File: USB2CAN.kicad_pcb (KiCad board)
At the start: 2 copper layers, 53.3 x 44.9 mm, 94 parts, among them J1 Conn_01x04, J2 Conn_01x02, J3 Conn_01x02, J4 Conn_01x02, J5 Conn_01x02, U1 HX9193, U10 SL2.1S, U2 STM32F072C8Tx, U3 TJA1051T-3, U4 STM32F072C8Tx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

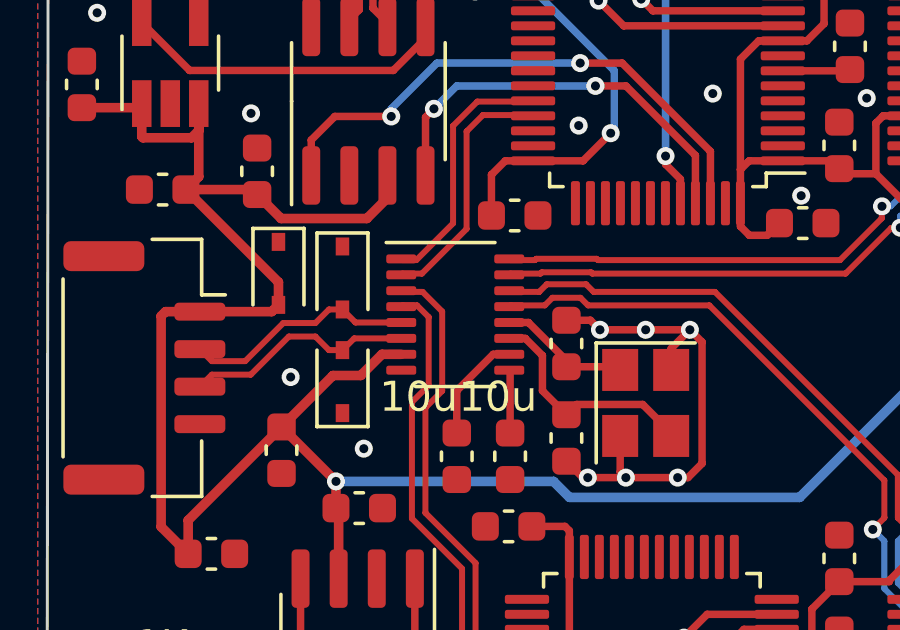
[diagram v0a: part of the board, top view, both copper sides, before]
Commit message: Turn overall Lib to local Lib to avoid incorrect display of schematics
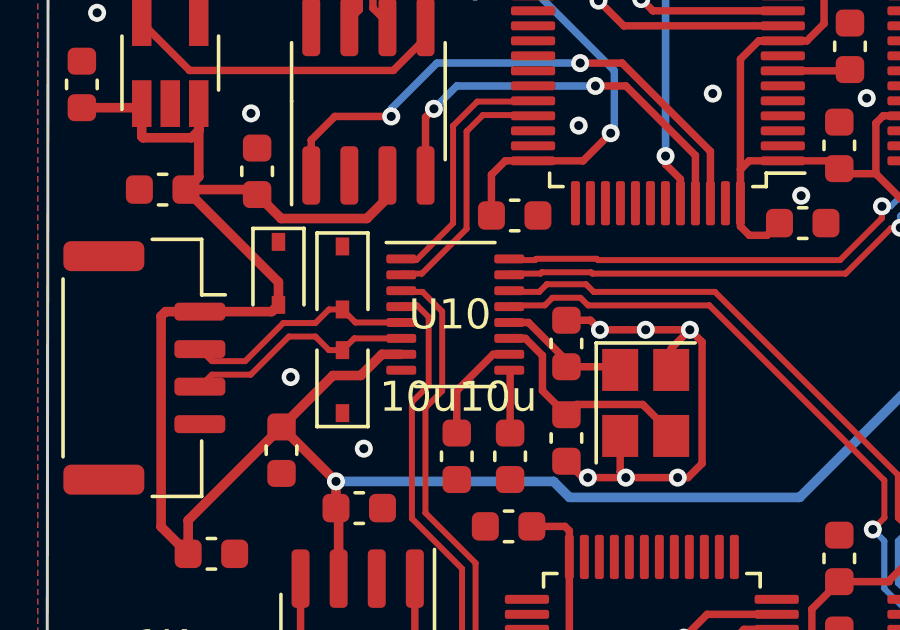
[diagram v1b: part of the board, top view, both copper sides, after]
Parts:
- removed REF** (x4): MountingHole_2.7mm_M2.5, MountingHole:MountingHole_2.7mm_M2.5
- added H1: MountingHole, MountingHole:MountingHole_2.7mm_M2.5, F.Cu at (85.2, 28.9)
- added H2: MountingHole, MountingHole:MountingHole_2.7mm_M2.5, F.Cu at (131.6, 28.9)
- added H3: MountingHole, MountingHole:MountingHole_2.7mm_M2.5, F.Cu at (131.6, 67.0)
- added H4: MountingHole, MountingHole:MountingHole_2.7mm_M2.5, F.Cu at (85.2, 67.0)
- U10: footprint MyLib:SL2.1S-SSOP-16 -> PcbLib:SL2.1S-SSOP-16
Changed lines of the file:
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@@
     )
   )
-  (footprint "MountingHole:MountingHole_2.7mm_M2.5" (layer "F.Cu")
-    (at 131.572 28.8544)
-    (descr "Mounting Hole 2.7mm, no annular, M2.5")
-    (tags "mounting hole 2.7mm no annular m2.5")
-    (attr exclude_from_pos_files exclude_from_bom)
-    (fp_text reference "REF**" (at 0 -3.7) (layer "F.SilkS") hide
-      (effects (font (size 1 1) (thickness 0.15)))
-    )
-    (fp_text value "MountingHole_2.7mm_M2.5" (at 0 3.7) (layer "F.Fab")
-      (effects (font (size 1 1) (thickness 0.15)))
-    )
-    (fp_text user "${REFERENCE}" (at 0.3 0) (layer "F.Fab")
-      (effects (font (size 1 1) (thickness 0.15)))
-    )
-    (fp_circle (center 0 0) (end 2.7 0) (layer "Cmts.User") (width 0.15) (fill none))
-    (fp_circle (center 0 0) (end 2.95 0) (layer "F.CrtYd") (width 0.05) (fill none))
-    (pad "" np_thru_hole circle locked (at 0 0) (size 2.7 2.7) (drill 2.7) (layers *.Cu *.Mask))
-  )
   (footprint "Resistor_SMD:R_0603_1608Metric" (layer "F.Cu")
     (at 102.0064 31.0388 180)
@@
     )
   )
-  (footprint "MyLib:SL2.1S-SSOP-16" (layer "F.Cu")
+  (footprint "PcbLib:SL2.1S-SSOP-16" (layer "F.Cu")
     (at 95.4532 45.8216)
     (property "Sheetfile" "USB_HUB.kicad_sch")
     (property "Sheetname" "USB_HUB")
     (attr smd)
-    (fp_text reference "U10" (at -0.175 0 unlocked) (layer "F.SilkS") hide
+    (fp_text reference "U10" (at -0.175 0 unlocked) (layer "F.SilkS")
       (effects (font (size 1 1) (thickness 0.15)))
     )
@@
     )
   )
+  (footprint "MountingHole:MountingHole_2.7mm_M2.5" (layer "F.Cu")
+    (at 85.1916 28.8544)
+    (descr "Mounting Hole 2.7mm, no annular, M2.5")
+    (tags "mounting hole 2.7mm no annular m2.5")
+    (property "Sheetfile" "USB2CAN.kicad_sch")
+    (property "Sheetname" "")
+    (attr exclude_from_pos_files)
+    (fp_text reference "H1" (at 0 -3.7) (layer "F.SilkS") hide
+      (effects (font (size 1 1) (thickness 0.15)))
+    )
+    (fp_text value "MountingHole" (at 0 3.7) (layer "F.Fab")
+      (effects (font (size 1 1) (thickness 0.15)))
+    )
+    (fp_text user "${REFERENCE}" (at 0.3 0) (layer "F.Fab")
+      (effects (font (size 1 1) (thickness 0.15)))
+    )
+    (fp_circle (center 0 0) (end 2.7 0) (layer "Cmts.User") (width 0.15) (fill none))
+    (fp_circle (center 0 0) (end 2.95 0) (layer "F.CrtYd") (width 0.05) (fill none))
+    (pad "" np_thru_hole circle locked (at 0 0) (size 2.7 2.7) (drill 2.7) (layers *.Cu *.Mask))
+  )
   (footprint "Connector_JST:JST_GH_SM02B-GHS-TB_1x02-1MP_P1.25mm_Horizontal" (layer "F.Cu")
     (at 92.202 67.4116)
@@
     )
   )
-  (footprint "MountingHole:MountingHole_2.7mm_M2.5" (layer "F.Cu")
-    (at 85.1916 66.9544)
-    (descr "Mounting Hole 2.7mm, no annular, M2.5")
-    (tags "mounting hole 2.7mm no annular m2.5")
-    (attr exclude_from_pos_files exclude_from_bom)
-    (fp_text reference "REF**" (at 0 -3.7) (layer "F.SilkS") hide
-      (effects (font (size 1 1) (thickness 0.15)))
-    )
-    (fp_text value "MountingHole_2.7mm_M2.5" (at 0 3.7) (layer "F.Fab")
-      (effects (font (size 1 1) (thickness 0.15)))
-    )
-    (fp_text user "${REFERENCE}" (at 0.3 0) (layer "F.Fab")
-      (effects (font (size 1 1) (thickness 0.15)))
-    )
-    (fp_circle (center 0 0) (end 2.7 0) (layer "Cmts.User") (width 0.15) (fill none))
-    (fp_circle (center 0 0) (end 2.95 0) (layer "F.CrtYd") (width 0.05) (fill none))
-    (pad "" np_thru_hole circle locked (at 0 0) (size 2.7 2.7) (drill 2.7) (layers *.Cu *.Mask))
-  )
   (footprint "Capacitor_SMD:C_0603_1608Metric" (layer "F.Cu")
     (at 85.6996 41.656 180)
@@
     )
   )
+  (footprint "MountingHole:MountingHole_2.7mm_M2.5" (layer "F.Cu")
+    (at 131.572 66.9544)
+    (descr "Mounting Hole 2.7mm, no annular, M2.5")
+    (tags "mounting hole 2.7mm no annular m2.5")
+    (property "Sheetfile" "USB2CAN.kicad_sch")
+    (property "Sheetname" "")
+    (attr exclude_from_pos_files)
+    (fp_text reference "H3" (at 0 -3.7) (layer "F.SilkS") hide
+      (effects (font (size 1 1) (thickness 0.15)))
+    )
+    (fp_text value "MountingHole" (at 0 3.7) (layer "F.Fab")
+      (effects (font (size 1 1) (thickness 0.15)))
+    )
+    (fp_text user "${REFERENCE}" (at 0.3 0) (layer "F.Fab")
+      (effects (font (size 1 1) (thickness 0.15)))
+    )
+    (fp_circle (center 0 0) (end 2.7 0) (layer "Cmts.User") (width 0.15) (fill none))
+    (fp_circle (center 0 0) (end 2.95 0) (layer "F.CrtYd") (width 0.05) (fill none))
+    (pad "" np_thru_hole circle locked (at 0 0) (size 2.7 2.7) (drill 2.7) (layers *.Cu *.Mask))
+  )
   (footprint "Capacitor_SMD:C_0603_1608Metric" (layer "F.Cu")
     (at 108.2548 53.9496 90)
@@
     )
   )
-  (footprint "MountingHole:MountingHole_2.7mm_M2.5" (layer "F.Cu")
-    (at 131.572 66.9544)
-    (descr "Mounting Hole 2.7mm, no annular, M2.5")
-    (tags "mounting hole 2.7mm no annular m2.5")
-    (attr exclude_from_pos_files exclude_from_bom)
-    (fp_text reference "REF**" (at 0 -3.7) (layer "F.SilkS") hide
-      (effects (font (size 1 1) (thickness 0.15)))
-    )
-    (fp_text value "MountingHole_2.7mm_M2.5" (at 0 3.7) (layer "F.Fab")
-      (effects (font (size 1 1) (thickness 0.15)))
-    )
-    (fp_text user "${REFERENCE}" (at 0.3 0) (layer "F.Fab")
-      (effects (font (size 1 1) (thickness 0.15)))
-    )
-    (fp_circle (center 0 0) (end 2.7 0) (layer "Cmts.User") (width 0.15) (fill none))
-    (fp_circle (center 0 0) (end 2.95 0) (layer "F.CrtYd") (width 0.05) (fill none))
-    (pad "" np_thru_hole circle locked (at 0 0) (size 2.7 2.7) (drill 2.7) (layers *.Cu *.Mask))
-  )
   (footprint "Package_QFP:LQFP-48_7x7mm_P0.5mm" (layer "F.Cu")
     (at 102.0064 58.0644 180)
@@
     )
   )
+  (footprint "MountingHole:MountingHole_2.7mm_M2.5" (layer "F.Cu")
+    (at 85.1916 66.9544)
+    (descr "Mounting Hole 2.7mm, no annular, M2.5")
+    (tags "mounting hole 2.7mm no annular m2.5")
+    (property "Sheetfile" "USB2CAN.kicad_sch")
+    (property "Sheetname" "")
+    (attr exclude_from_pos_files)
+    (fp_text reference "H4" (at 0 -3.7) (layer "F.SilkS") hide
+      (effects (font (size 1 1) (thickness 0.15)))
+    )
+    (fp_text value "MountingHole" (at 0 3.7) (layer "F.Fab")
+      (effects (font (size 1 1) (thickness 0.15)))
+    )
+    (fp_text user "${REFERENCE}" (at 0.3 0) (layer "F.Fab")
+      (effects (font (size 1 1) (thickness 0.15)))
+    )
+    (fp_circle (center 0 0) (end 2.7 0) (layer "Cmts.User") (width 0.15) (fill none))
+    (fp_circle (center 0 0) (end 2.95 0) (layer "F.CrtYd") (width 0.05) (fill none))
+    (pad "" np_thru_hole circle locked (at 0 0) (size 2.7 2.7) (drill 2.7) (layers *.Cu *.Mask))
+  )
   (footprint "Resistor_SMD:R_0603_1608Metric" (layer "F.Cu")
     (at 124.206 33.6804)
@@
     )
   )
-  (footprint "MountingHole:MountingHole_2.7mm_M2.5" (layer "F.Cu")
-    (at 85.1916 28.8544)
-    (descr "Mounting Hole 2.7mm, no annular, M2.5")
-    (tags "mounting hole 2.7mm no annular m2.5")
-    (attr exclude_from_pos_files exclude_from_bom)
-    (fp_text reference "REF**" (at 0 -3.7) (layer "F.SilkS") hide
-      (effects (font (size 1 1) (thickness 0.15)))
-    )
-    (fp_text value "MountingHole_2.7mm_M2.5" (at 0 3.7) (layer "F.Fab")
-      (effects (font (size 1 1) (thickness 0.15)))
-    )
-    (fp_text user "${REFERENCE}" (at 0.3 0) (layer "F.Fab")
-      (effects (font (size 1 1) (thickness 0.15)))
-    )
-    (fp_circle (center 0 0) (end 2.7 0) (layer "Cmts.User") (width 0.15) (fill none))
-    (fp_circle (center 0 0) (end 2.95 0) (layer "F.CrtYd") (width 0.05) (fill none))
-    (pad "" np_thru_hole circle locked (at 0 0) (size 2.7 2.7) (drill 2.7) (layers *.Cu *.Mask))
-  )
   (footprint "Capacitor_SMD:C_0603_1608Metric" (layer "F.Cu")
     (at 108.2548 60.2488 90)
@@
     )
   )
+  (footprint "MountingHole:MountingHole_2.7mm_M2.5" (layer "F.Cu")
+    (at 131.572 28.8544)
+    (descr "Mounting Hole 2.7mm, no annular, M2.5")
+    (tags "mounting hole 2.7mm no annular m2.5")
+    (property "Sheetfile" "USB2CAN.kicad_sch")
+    (property "Sheetname" "")
+    (attr exclude_from_pos_files)
+    (fp_text reference "H2" (at 0 -3.7) (layer "F.SilkS") hide
+      (effects (font (size 1 1) (thickness 0.15)))
+    )
+    (fp_text value "MountingHole" (at 0 3.7) (layer "F.Fab")
+      (effects (font (size 1 1) (thickness 0.15)))
+    )
+    (fp_text user "${REFERENCE}" (at 0.3 0) (layer "F.Fab")
+      (effects (font (size 1 1) (thickness 0.15)))
+    )
+    (fp_circle (center 0 0) (end 2.7 0) (layer "Cmts.User") (width 0.15) (fill none))
+    (fp_circle (center 0 0) (end 2.95 0) (layer "F.CrtYd") (width 0.05) (fill none))
+    (pad "" np_thru_hole circle locked (at 0 0) (size 2.7 2.7) (drill 2.7) (layers *.Cu *.Mask))
+  )
   (footprint "Capacitor_SMD:C_0603_1608Metric" (layer "F.Cu")
